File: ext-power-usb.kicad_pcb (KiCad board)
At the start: 2 copper layers, 17.8 x 48.3 mm, 6 parts, among them J1 USB_A, J2 USB_A, U1 L7805

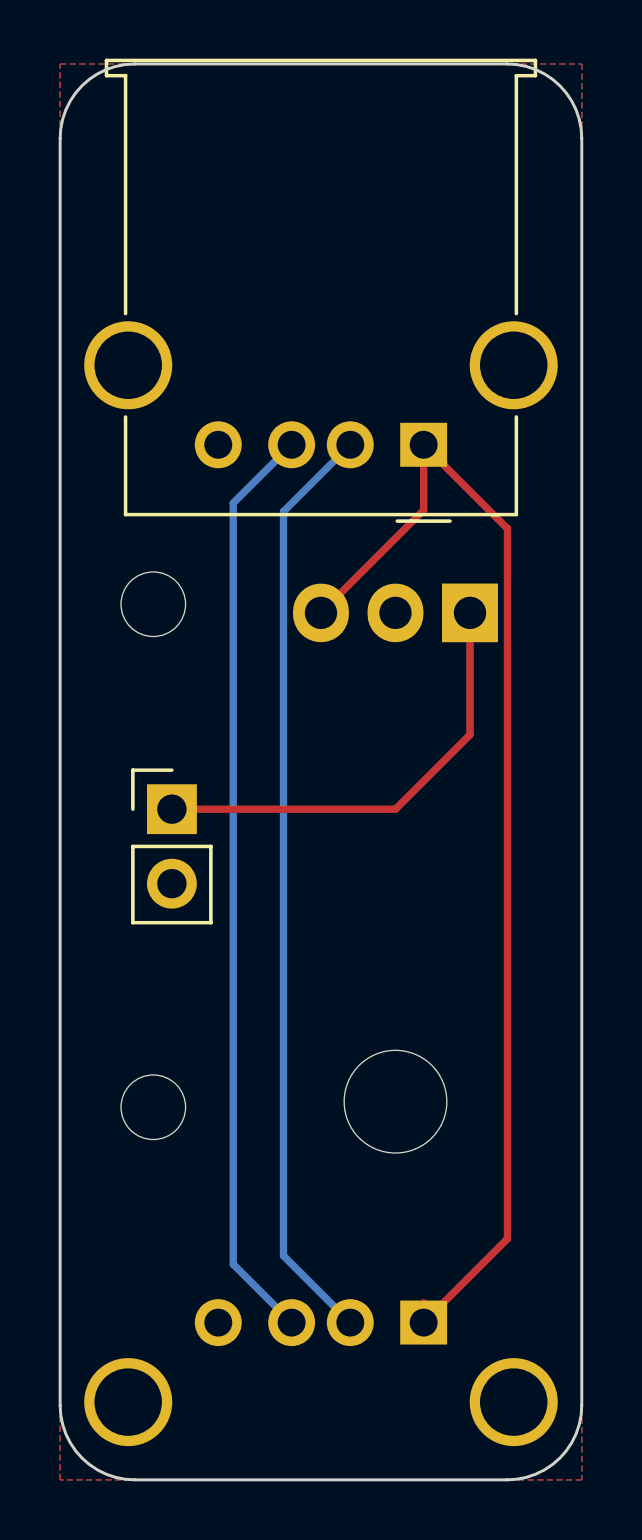
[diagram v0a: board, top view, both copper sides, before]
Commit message: Shifted USB plug deeper onto board, adjusted position of input power
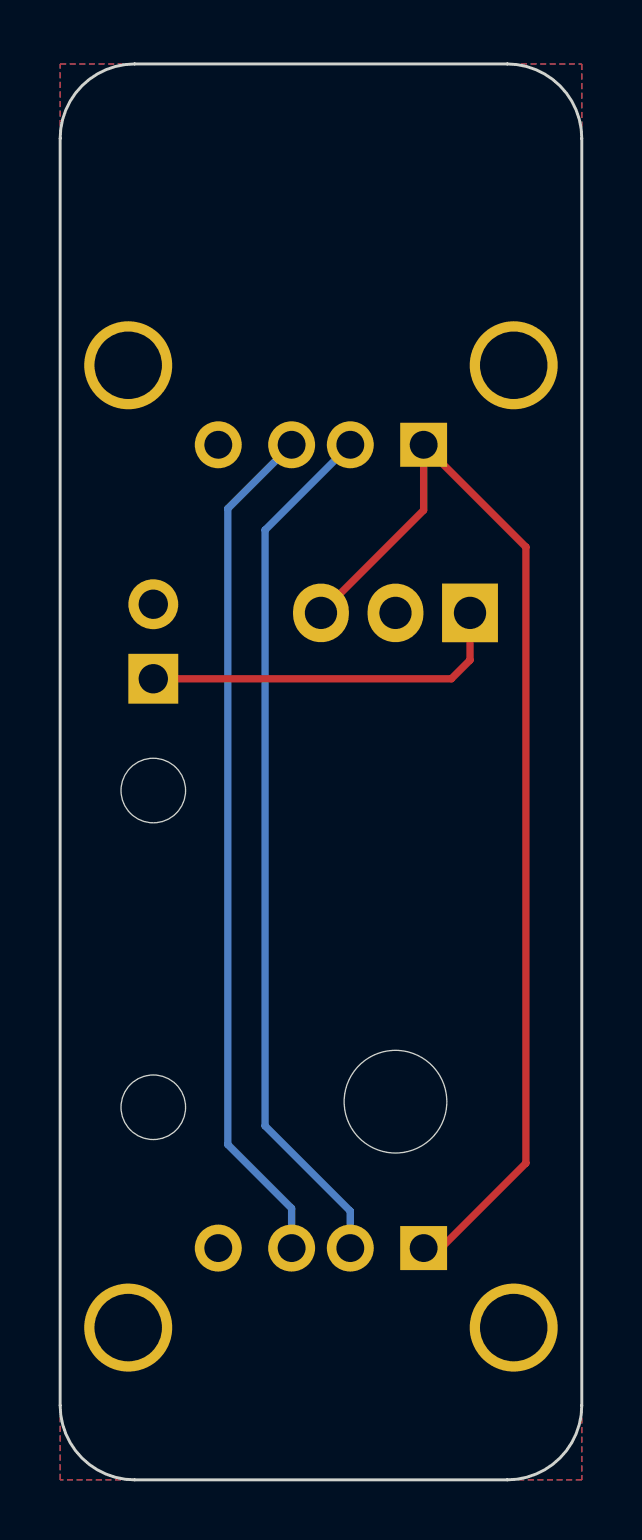
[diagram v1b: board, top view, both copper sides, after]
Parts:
- moved REF** 6.35 mm to (126.4, 55.2)
- moved BT1 4.49 mm to (126.4, 51.4), turned to 180 degrees
- moved J1 2.54 mm to (135.6, 70.8)
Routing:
- net Net-(BT1-Pad1): track 15.4 -> 12.7 mm
- net Net-(J1-Pad3): track 31.6 -> 29.2 mm
- net Net-(J1-Pad1): track 40.1 -> 37.8 mm
- net Net-(J1-Pad2): track 31.8 -> 29.8 mm
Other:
- board text added: "Ext Power USB Version 1.1 Liam Fruzyna FRC 111/112"
- board text removed: "Ext Power USB Version 1.0 Liam Fruzyna FRC 111/112"
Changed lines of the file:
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@@
       (effects (font (size 1 1) (thickness 0.15)))
     )
-    (fp_line (start 10.16 -2.38) (end 10.16 0.95) (layer "F.SilkS") (width 0.12))
-    (fp_line (start -3.81 13.1) (end 10.81 13.1) (layer "F.SilkS") (width 0.12))
-    (fp_line (start 10.81 12.58) (end 10.16 12.58) (layer "F.SilkS") (width 0.12))
-    (fp_line (start 10.16 4.47) (end 10.16 12.58) (layer "F.SilkS") (width 0.12))
-    (fp_line (start -3.16 12.58) (end -3.16 4.47) (layer "F.SilkS") (width 0.12))
-    (fp_line (start -3.81 12.58) (end -3.81 13.1) (layer "F.SilkS") (width 0.12))
-    (fp_line (start -0.9 -2.6) (end 0.9 -2.6) (layer "F.SilkS") (width 0.12))
-    (fp_line (start -3.16 -2.38) (end 10.16 -2.38) (layer "F.SilkS") (width 0.12))
-    (fp_line (start 10.81 13.1) (end 10.81 12.58) (layer "F.SilkS") (width 0.12))
-    (fp_line (start -3.16 12.58) (end -3.81 12.58) (layer "F.SilkS") (width 0.12))
-    (fp_line (start -3.16 -2.38) (end -3.16 0.95) (layer "F.SilkS") (width 0.12))
     (fp_line (start 10.55 12.19) (end 10.55 4.66) (layer "F.CrtYd") (width 0.05))
     (fp_line (start 10.55 -2.77) (end 10.55 0.76) (layer "F.CrtYd") (width 0.05))
@@
   )
   (footprint "MountingHole:MountingHole_2.2mm_M2_ISO7380" (layer "F.Cu")
-    (at 126.365 48.895)
+    (at 126.365 55.245)
     (descr "Mounting Hole 2.2mm, no annular, M2, ISO7380")
     (tags "mounting hole 2.2mm no annular m2 iso7380")
@@
   )
   (footprint "Connector_PinHeader_2.54mm:PinHeader_1x02_P2.54mm_Vertical" (layer "F.Cu")
-    (at 127 55.88)
+    (at 126.365 51.435 180)
     (descr "Through hole straight pin header, 1x02, 2.54mm pitch, single row")
     (tags "Through hole pin header THT 1x02 2.54mm single row")
@@
       (effects (font (size 1 1) (thickness 0.15)))
     )
-    (fp_line (start -1.33 1.27) (end 1.33 1.27) (layer "F.SilkS") (width 0.12))
-    (fp_line (start -1.33 3.87) (end 1.33 3.87) (layer "F.SilkS") (width 0.12))
-    (fp_line (start -1.33 1.27) (end -1.33 3.87) (layer "F.SilkS") (width 0.12))
-    (fp_line (start 1.33 1.27) (end 1.33 3.87) (layer "F.SilkS") (width 0.12))
-    (fp_line (start -1.33 -1.33) (end 0 -1.33) (layer "F.SilkS") (width 0.12))
-    (fp_line (start -1.33 0) (end -1.33 -1.33) (layer "F.SilkS") (width 0.12))
     (fp_line (start 1.8 4.35) (end 1.8 -1.8) (layer "F.CrtYd") (width 0.05))
     (fp_line (start 1.8 -1.8) (end -1.8 -1.8) (layer "F.CrtYd") (width 0.05))
@@
     (fp_line (start 1.27 3.81) (end -1.27 3.81) (layer "F.Fab") (width 0.1))
     (fp_line (start -1.27 3.81) (end -1.27 -0.635) (layer "F.Fab") (width 0.1))
-    (pad "1" thru_hole rect (at 0 0) (size 1.7 1.7) (drill 1) (layers *.Cu *.Mask)
+    (pad "1" thru_hole rect (at 0 0 180) (size 1.7 1.7) (drill 1) (layers *.Cu *.Mask)
       (net 1 "Net-(BT1-Pad1)") (pinfunction "+") (pintype "passive"))
-    (pad "2" thru_hole oval (at 0 2.54) (size 1.7 1.7) (drill 1) (layers *.Cu *.Mask)
+    (pad "2" thru_hole oval (at 0 2.54 180) (size 1.7 1.7) (drill 1) (layers *.Cu *.Mask)
       (net 2 "Net-(J1-Pad4)") (pinfunction "-") (pintype "passive"))
     (model "${KICAD6_3DMODEL_DIR}/Connector_PinHeader_2.54mm.3dshapes/PinHeader_1x02_P2.54mm_Vertical.wrl"
@@
   )
   (footprint "Connector_USB:USB_A_Molex_67643_Horizontal" (layer "B.Cu")
-    (at 135.58 73.38 180)
+    (at 135.58 70.84 180)
     (descr "USB type A, Horizontal, https://www.molex.com/pdm_docs/sd/676433910_sd.pdf")
     (tags "USB_A Female Connector receptacle")
@@
       (effects (font (size 1 1) (thickness 0.15)) (justify mirror))
     )
-    (fp_line (start -3.16 -12.58) (end -3.81 -12.58) (layer "B.SilkS") (width 0.12))
-    (fp_line (start -3.16 -12.58) (end -3.16 -4.47) (layer "B.SilkS") (width 0.12))
-    (fp_line (start -3.16 2.38) (end -3.16 -0.95) (layer "B.SilkS") (width 0.12))
-    (fp_line (start 10.81 -12.58) (end 10.16 -12.58) (layer "B.SilkS") (width 0.12))
-    (fp_line (start 10.81 -13.1) (end 10.81 -12.58) (layer "B.SilkS") (width 0.12))
-    (fp_line (start 10.16 -4.47) (end 10.16 -12.58) (layer "B.SilkS") (width 0.12))
-    (fp_line (start -0.9 2.6) (end 0.9 2.6) (layer "B.SilkS") (width 0.12))
-    (fp_line (start -3.81 -13.1) (end 10.81 -13.1) (layer "B.SilkS") (width 0.12))
-    (fp_line (start -3.16 2.38) (end 10.16 2.38) (layer "B.SilkS") (width 0.12))
-    (fp_line (start 10.16 2.38) (end 10.16 -0.95) (layer "B.SilkS") (width 0.12))
-    (fp_line (start -3.81 -12.58) (end -3.81 -13.1) (layer "B.SilkS") (width 0.12))
     (fp_line (start -4.2 -12.19) (end -3.55 -12.19) (layer "B.CrtYd") (width 0.05))
     (fp_line (start -3.55 -12.19) (end -3.55 -4.66) (layer "B.CrtYd") (width 0.05))
@@
       (effects (font (size 1 1) (thickness 0.15)) (justify mirror))
     )
-    (fp_line (start 7.66 -15.82) (end 7.66 -17.02) (layer "B.SilkS") (width 0.12))
-    (fp_line (start -2.58 -13.42) (end -2.58 -14.62) (layer "B.SilkS") (width 0.12))
-    (fp_line (start -2.58 -18.22) (end -2.58 -19.42) (layer "B.SilkS") (width 0.12))
-    (fp_line (start -2.58 -3.69) (end 7.66 -3.69) (layer "B.SilkS") (width 0.12))
-    (fp_line (start -2.58 -3.69) (end -2.58 -13.18) (layer "B.SilkS") (width 0.12))
-    (fp_line (start 7.02 -19.58) (end 7.66 -19.58) (layer "B.SilkS") (width 0.12))
-    (fp_line (start -2.58 -15.82) (end -2.58 -17.02) (layer "B.SilkS") (width 0.12))
-    (fp_line (start -0.181 -19.58) (end 1.02 -19.58) (layer "B.SilkS") (width 0.12))
-    (fp_line (start 2.54 -1.15) (end 2.54 -3.69) (layer "B.SilkS") (width 0.12))
-    (fp_line (start -2.58 -13.18) (end 7.66 -13.18) (layer "B.SilkS") (width 0.12))
-    (fp_line (start 7.66 -3.69) (end 7.66 -13.18) (layer "B.SilkS") (width 0.12))
-    (fp_line (start 2.22 -19.58) (end 3.42 -19.58) (layer "B.SilkS") (width 0.12))
-    (fp_line (start 7.66 -13.42) (end 7.66 -14.62) (layer "B.SilkS") (width 0.12))
-    (fp_line (start 4.62 -19.58) (end 5.82 -19.58) (layer "B.SilkS") (width 0.12))
-    (fp_line (start 5.08 -1.15) (end 5.08 -3.69) (layer "B.SilkS") (width 0.12))
-    (fp_line (start 0 -1.15) (end 0 -3.69) (layer "B.SilkS") (width 0.12))
-    (fp_line (start 7.66 -18.22) (end 7.66 -19.42) (layer "B.SilkS") (width 0.12))
-    (fp_line (start -2.58 -19.58) (end -1.38 -19.58) (layer "B.SilkS") (width 0.12))
     (fp_line (start 7.79 1.25) (end -2.71 1.25) (layer "B.CrtYd") (width 0.05))
     (fp_line (start -2.71 1.25) (end -2.71 -19.71) (layer "B.CrtYd") (width 0.05))
@@
   (gr_line (start 140.97 33.02) (end 140.97 76.2) (layer "Edge.Cuts") (width 0.1))
   (gr_arc (start 140.97 76.2) (mid 140.226051 77.996051) (end 138.43 78.74) (layer "Edge.Cuts") (width 0.1))
-  (gr_text "Ext Power USB\nVersion 1.0\nLiam Fruzyna\nFRC 111/112" (at 132.08 35.56) (layer "B.SilkS")
+  (gr_text "Ext Power USB\nVersion 1.1\nLiam Fruzyna\nFRC 111/112" (at 132.08 35.56) (layer "B.SilkS")
     (effects (font (size 1 1) (thickness 0.15)) (justify mirror))
   )
-  (segment (start 127 55.88) (end 134.62 55.88) (width 0.25) (layer "F.Cu") (net 1))
-  (segment (start 137.16 53.34) (end 137.16 49.19) (width 0.25) (layer "F.Cu") (net 1))
-  (segment (start 134.62 55.88) (end 137.16 53.34) (width 0.25) (layer "F.Cu") (net 1))
-  (segment (start 138.4375 46.3175) (end 138.4375 70.5225) (width 0.25) (layer "F.Cu") (net 3))
+  (segment (start 136.525 51.435) (end 137.16 50.8) (width 0.25) (layer "F.Cu") (net 1))
+  (segment (start 137.16 50.8) (end 137.16 49.19) (width 0.25) (layer "F.Cu") (net 1))
+  (segment (start 126.365 51.435) (end 136.525 51.435) (width 0.25) (layer "F.Cu") (net 1))
+  (segment (start 135.58 43.46) (end 139.065 46.945) (width 0.25) (layer "F.Cu") (net 3))
   (segment (start 135.58 43.46) (end 135.58 45.69) (width 0.25) (layer "F.Cu") (net 3))
   (segment (start 135.58 45.69) (end 132.08 49.19) (width 0.25) (layer "F.Cu") (net 3))
-  (segment (start 135.58 43.46) (end 138.4375 46.3175) (width 0.25) (layer "F.Cu") (net 3))
-  (segment (start 135.58 73.38) (end 135.58 72.7) (width 0.25) (layer "F.Cu") (net 3))
-  (segment (start 138.4375 70.5225) (end 135.58 73.38) (width 0.25) (layer "F.Cu") (net 3))
-  (segment (start 130.8025 71.1025) (end 133.08 73.38) (width 0.25) (layer "B.Cu") (net 4))
-  (segment (start 130.8025 45.7375) (end 130.8025 71.1025) (width 0.25) (layer "B.Cu") (net 4))
-  (segment (start 133.08 43.46) (end 130.8025 45.7375) (width 0.25) (layer "B.Cu") (net 4))
-  (segment (start 129.09 71.39) (end 131.08 73.38) (width 0.25) (layer "B.Cu") (net 5))
-  (segment (start 129.09 45.45) (end 129.09 71.39) (width 0.25) (layer "B.Cu") (net 5))
-  (segment (start 131.08 43.46) (end 129.09 45.45) (width 0.25) (layer "B.Cu") (net 5))
+  (segment (start 139.065 67.945) (end 136.17 70.84) (width 0.25) (layer "F.Cu") (net 3))
+  (segment (start 139.065 46.945) (end 139.065 67.945) (width 0.25) (layer "F.Cu") (net 3))
+  (segment (start 136.17 70.84) (end 135.58 70.84) (width 0.25) (layer "F.Cu") (net 3))
+  (segment (start 133.08 69.58) (end 133.08 70.84) (width 0.25) (layer "B.Cu") (net 4))
+  (segment (start 130.175 66.675) (end 133.08 69.58) (width 0.25) (layer "B.Cu") (net 4))
+  (segment (start 133.08 43.46) (end 130.175 46.365) (width 0.25) (layer "B.Cu") (net 4))
+  (segment (start 130.175 46.365) (end 130.175 66.675) (width 0.25) (layer "B.Cu") (net 4))
+  (segment (start 131.08 69.485) (end 131.08 70.84) (width 0.25) (layer "B.Cu") (net 5))
+  (segment (start 131.08 43.46) (end 128.905 45.635) (width 0.25) (layer "B.Cu") (net 5))
+  (segment (start 128.905 67.31) (end 131.08 69.485) (width 0.25) (layer "B.Cu") (net 5))
+  (segment (start 128.905 45.635) (end 128.905 67.31) (width 0.25) (layer "B.Cu") (net 5))
   (zone (net 2) (net_name "Net-(J1-Pad4)") (layers F&B.Cu) (hatch edge 0.508)
     (connect_pads (clearance 0.508))
